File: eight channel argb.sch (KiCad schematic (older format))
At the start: 13 parts, among them J1 Conn_01x03, J10 Conn_01x06_Male, J2 Conn_01x03, J3 Conn_01x03, J4 Conn_01x03, J5 Conn_01x03, J6 Conn_01x03, J7 Conn_01x03, J8 Conn_01x03, J9 Conn_01x06_Male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

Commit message: Remove 6-pin SATA power connectors and replace with 4-pin "Molex" socket.
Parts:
- removed J10, J9: Conn_01x06_Male, Connector_JST:JST_XH_S6B-XH-A_1x06_P2.50mm_Horizontal, symbol Connector:Conn_01x06_Male
- added J?: 350211-1, 3502111, symbol SamacSys:350211-1
- J1, J2, J3, J4, J5, J6, J7, J8: symbol Connector_Generic:Conn_01x03 -> eight-channel-argb-rescue:Conn_01x03-Connector_Generic
- SW1: symbol Switch:SW_DIP_x01 -> eight-channel-argb-rescue:SW_DIP_x01-Switch
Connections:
- wire segments 138 -> 113
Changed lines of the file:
@@
 $EndComp
 $Comp
-L Connector_Generic:Conn_01x03 J2
+L eight-channel-argb-rescue:Conn_01x03-Connector_Generic J2
 U 1 1 5FF2A38F
 P 7350 2600
@@
 F 3 "https://aliexpress.com/item/32864722159.html" H 2800 5150 50  0001 C CNN
 	1    3250 3800
-	1    0    0    -1
-$EndComp
-$Comp
-L power:+5V #PWR01
-U 1 1 5FF37571
-P 4700 1500
-F 0 "#PWR01" H 4700 1350 50  0001 C CNN
-F 1 "+5V" H 4715 1673 50  0000 C CNN
-F 2 "" H 4700 1500 50  0001 C CNN
-F 3 "" H 4700 1500 50  0001 C CNN
-	1    4700 1500
-	1    0    0    -1
-$EndComp
-$Comp
-L power:GND #PWR02
-U 1 1 5FF37BFD
-P 5200 1200
-F 0 "#PWR02" H 5200 950 50  0001 C CNN
-F 1 "GND" H 5205 1027 50  0000 C CNN
-F 2 "" H 5200 1200 50  0001 C CNN
-F 3 "" H 5200 1200 50  0001 C CNN
-	1    5200 1200
 	1    0    0    -1
 $EndComp
@@
 NoConn ~ 3250 5200
 $Comp
-L Connector_Generic:Conn_01x03 J1
+L eight-channel-argb-rescue:Conn_01x03-Connector_Generic J1
 U 1 1 5FF476B4
 P 7350 2200
@@
 $EndComp
 $Comp
-L Connector_Generic:Conn_01x03 J7
+L eight-channel-argb-rescue:Conn_01x03-Connector_Generic J7
 U 1 1 5FF47C5F
 P 7350 4600
@@
 $EndComp
 $Comp
-L Connector_Generic:Conn_01x03 J6
+L eight-channel-argb-rescue:Conn_01x03-Connector_Generic J6
 U 1 1 5FF4879A
 P 7350 4200
@@
 $EndComp
 $Comp
-L Connector_Generic:Conn_01x03 J5
+L eight-channel-argb-rescue:Conn_01x03-Connector_Generic J5
 U 1 1 5FF48D18
 P 7350 3800
@@
 $EndComp
 $Comp
-L Connector_Generic:Conn_01x03 J4
+L eight-channel-argb-rescue:Conn_01x03-Connector_Generic J4
 U 1 1 5FF49041
 P 7350 3400
@@
 $EndComp
 $Comp
-L Connector_Generic:Conn_01x03 J3
+L eight-channel-argb-rescue:Conn_01x03-Connector_Generic J3
 U 1 1 5FF495A2
 P 7350 3000
@@
 $EndComp
 $Comp
-L Connector_Generic:Conn_01x03 J8
+L eight-channel-argb-rescue:Conn_01x03-Connector_Generic J8
 U 1 1 5FF4A43D
 P 7350 5000
@@
 	6900 5100 7150 5100
 Wire Wire Line
-	4950 2100 5200 2100
-Wire Wire Line
 	7150 4700 6900 4700
 Connection ~ 6900 4700
@@
 Wire Wire Line
 	6350 5000 6350 3750
-$Comp
-L power:PWR_FLAG #FLG02
-U 1 1 5FF6F199
-P 4700 1850
-F 0 "#FLG02" H 4700 1925 50  0001 C CNN
-F 1 "PWR_FLAG" H 4450 1850 50  0000 C CNN
-F 2 "" H 4700 1850 50  0001 C CNN
-F 3 "~" H 4700 1850 50  0001 C CNN
-	1    4700 1850
-	1    0    0    -1
-$EndComp
 Wire Wire Line
 	4550 2150 4700 2150
-Wire Wire Line
-	4700 1500 4700 1850
-Connection ~ 4700 1850
-Wire Wire Line
-	4700 1850 4700 1950
-Wire Wire Line
-	7000 1850 6700 1850
 Wire Wire Line
 	4900 1850 4900 1950
@@
 	4900 1950 4700 1950
 Connection ~ 4700 1950
-Wire Wire Line
-	4700 1950 4700 2150
-Wire Wire Line
-	5200 1550 5200 1650
-Connection ~ 5200 2100
-Wire Wire Line
-	5200 1550 5450 1550
-Wire Wire Line
-	5450 1550 5450 1500
-Wire Wire Line
-	5450 1200 5200 1200
-$Comp
-L power:PWR_FLAG #FLG03
-U 1 1 5FF8D592
-P 5450 1500
-F 0 "#FLG03" H 5450 1575 50  0001 C CNN
-F 1 "PWR_FLAG" H 5200 1500 50  0000 C CNN
-F 2 "" H 5450 1500 50  0001 C CNN
-F 3 "~" H 5450 1500 50  0001 C CNN
-	1    5450 1500
-	1    0    0    -1
-$EndComp
-Connection ~ 5450 1500
-Wire Wire Line
-	5450 1500 5450 1200
-Connection ~ 6700 1850
-Wire Wire Line
-	6800 1700 6800 2100
-Connection ~ 6800 2100
-Wire Wire Line
-	6800 2100 6900 2100
-$Comp
-L Switch:SW_DIP_x01 SW1
+$Comp
+L eight-channel-argb-rescue:SW_DIP_x01-Switch SW1
 U 1 1 5FFD2886
 P 3800 1950
@@
 	4100 1950 4700 1950
 $Comp
-L power:PWR_FLAG #FLG01
+L eight-channel-argb-rescue:PWR_FLAG-power #FLG01
 U 1 1 5FF41B16
 P 3250 1950
@@
 	3250 1950 3500 1950
 $Comp
-L Connector:Conn_01x06_Male J9
-U 1 1 5FF69EE1
-P 6050 1200
-F 0 "J9" V 6112 1444 50  0000 L CNN
-F 1 "Conn_01x06_Male" V 6203 1444 50  0000 L CNN
-F 2 "Connector_JST:JST_XH_S6B-XH-A_1x06_P2.50mm_Horizontal" H 6050 1200 50  0001 C CNN
-F 3 "~" H 6050 1200 50  0001 C CNN
-	1    6050 1200
-	0    1    1    0
-$EndComp
-$Comp
-L Connector:Conn_01x06_Male J10
-U 1 1 5FF6B11B
-P 7400 1200
-F 0 "J10" V 7462 1444 50  0000 L CNN
-F 1 "Conn_01x06_Male" V 7553 1444 50  0000 L CNN
-F 2 "Connector_JST:JST_XH_S6B-XH-A_1x06_P2.50mm_Horizontal" H 7400 1200 50  0001 C CNN
-F 3 "~" H 7400 1200 50  0001 C CNN
-	1    7400 1200
-	0    1    1    0
-$EndComp
-Wire Wire Line
-	6700 1600 6700 1850
-Wire Wire Line
-	5200 2100 6800 2100
-Wire Wire Line
-	4900 1850 6700 1850
-Wire Wire Line
-	6700 1600 6250 1600
-Wire Wire Line
-	6050 1600 6050 1400
-Wire Wire Line
-	6150 1600 6150 1400
-Connection ~ 6150 1600
-Wire Wire Line
-	6150 1600 6050 1600
-Wire Wire Line
-	6250 1600 6250 1400
-Connection ~ 6250 1600
-Wire Wire Line
-	6250 1600 6150 1600
-Wire Wire Line
-	5200 1650 5750 1650
-Wire Wire Line
-	5750 1650 5750 1400
-Connection ~ 5200 1650
-Wire Wire Line
-	5200 1650 5200 2100
-Wire Wire Line
-	5750 1650 5850 1650
-Wire Wire Line
-	5850 1650 5850 1400
-Connection ~ 5750 1650
-Wire Wire Line
-	5850 1650 5950 1650
-Wire Wire Line
-	5950 1650 5950 1400
-Connection ~ 5850 1650
-Wire Wire Line
-	6800 1700 7100 1700
-Wire Wire Line
-	7100 1700 7100 1450
-Wire Wire Line
-	7100 1450 7200 1450
-Wire Wire Line
-	7200 1450 7200 1400
-Connection ~ 7100 1450
-Wire Wire Line
-	7100 1450 7100 1400
-Wire Wire Line
-	7200 1450 7300 1450
-Wire Wire Line
-	7300 1450 7300 1400
-Connection ~ 7200 1450
-Wire Wire Line
-	7000 1850 7400 1850
-Wire Wire Line
-	7400 1850 7400 1400
-Connection ~ 7000 1850
-Wire Wire Line
-	7400 1400 7500 1400
-Connection ~ 7400 1400
-Wire Wire Line
-	7400 1400 7500 1400
-Connection ~ 7500 1400
-Wire Wire Line
-	7500 1400 7600 1400
+L SamacSys:350211-1 J?
+U 1 1 6053820E
+P 5300 1300
+F 0 "J?" H 5928 1196 50  0000 L CNN
+F 1 "350211-1" H 5928 1105 50  0000 L CNN
+F 2 "3502111" H 5950 1400 50  0001 L CNN
+F 3 "http://uk.rs-online.com/web/p/products/0471430" H 5950 1300 50  0001 L CNN
+F 4 "Pin & Socket Connectors CONN PCM 4 POS TIN" H 5950 1200 50  0001 L CNN "Description"
+F 5 "10.29" H 5950 1100 50  0001 L CNN "Height"
+F 6 "0471430" H 5950 1000 50  0001 L CNN "RS Part Number"
+F 7 "http://uk.rs-online.com/web/p/products/0471430" H 5950 900 50  0001 L CNN "RS Price/Stock"
+F 8 "TE Connectivity" H 5950 800 50  0001 L CNN "Manufacturer_Name"
+F 9 "350211-1" H 5950 700 50  0001 L CNN "Manufacturer_Part_Number"
+	1    5300 1300
+	1    0    0    -1
+$EndComp
+Wire Wire Line
+	4900 1850 5000 1850
+Connection ~ 5200 2100
+Wire Wire Line
+	5200 2100 6900 2100
+Wire Wire Line
+	4950 2100 5200 2100
+Wire Wire Line
+	4700 1950 4700 2150
+Connection ~ 5000 1850
+Wire Wire Line
+	5000 1850 7000 1850
+Wire Wire Line
+	5300 1600 5000 1600
+Wire Wire Line
+	5300 1500 5200 1500
+Connection ~ 5200 1500
+Wire Wire Line
+	5300 1400 5200 1400
+Wire Wire Line
+	5200 1400 5200 1500
+Wire Wire Line
+	5200 1500 5200 2100
+Wire Wire Line
+	5000 1600 5000 1850
+$Comp
+L eight-channel-argb-rescue:PWR_FLAG-power #FLG03
+U 1 1 5FF8D592
+P 5200 1050
+F 0 "#FLG03" H 5200 1125 50  0001 C CNN
+F 1 "PWR_FLAG" H 4950 1050 50  0000 C CNN
+F 2 "" H 5200 1050 50  0001 C CNN
+F 3 "~" H 5200 1050 50  0001 C CNN
+	1    5200 1050
+	1    0    0    -1
+$EndComp
+Connection ~ 5200 1050
+Connection ~ 5000 950
+Wire Wire Line
+	5200 1050 5200 1400
+Wire Wire Line
+	5000 950  5000 1600
+$Comp
+L eight-channel-argb-rescue:GND-power #PWR02
+U 1 1 5FF37BFD
+P 5200 850
+F 0 "#PWR02" H 5200 600 50  0001 C CNN
+F 1 "GND" H 5205 677 50  0000 C CNN
+F 2 "" H 5200 850 50  0001 C CNN
+F 3 "" H 5200 850 50  0001 C CNN
+	1    5200 850
+	-1   0    0    1
+$EndComp
+$Comp
+L eight-channel-argb-rescue:PWR_FLAG-power #FLG02
+U 1 1 5FF6F199
+P 5000 950
+F 0 "#FLG02" H 5000 1025 50  0001 C CNN
+F 1 "PWR_FLAG" H 4750 950 50  0000 C CNN
+F 2 "" H 5000 950 50  0001 C CNN
+F 3 "~" H 5000 950 50  0001 C CNN
+	1    5000 950
+	1    0    0    -1
+$EndComp
+Wire Wire Line
+	5200 1050 5200 850
+Wire Wire Line
+	5000 850  5000 950
+$Comp
+L eight-channel-argb-rescue:+5V-power #PWR01
+U 1 1 5FF37571
+P 5000 850
+F 0 "#PWR01" H 5000 700 50  0001 C CNN
+F 1 "+5V" H 5015 1023 50  0000 C CNN
+F 2 "" H 5000 850 50  0001 C CNN
+F 3 "" H 5000 850 50  0001 C CNN
+	1    5000 850
+	1    0    0    -1
+$EndComp
+Connection ~ 5200 1400
+Connection ~ 5000 1600
 $EndSCHEMATC

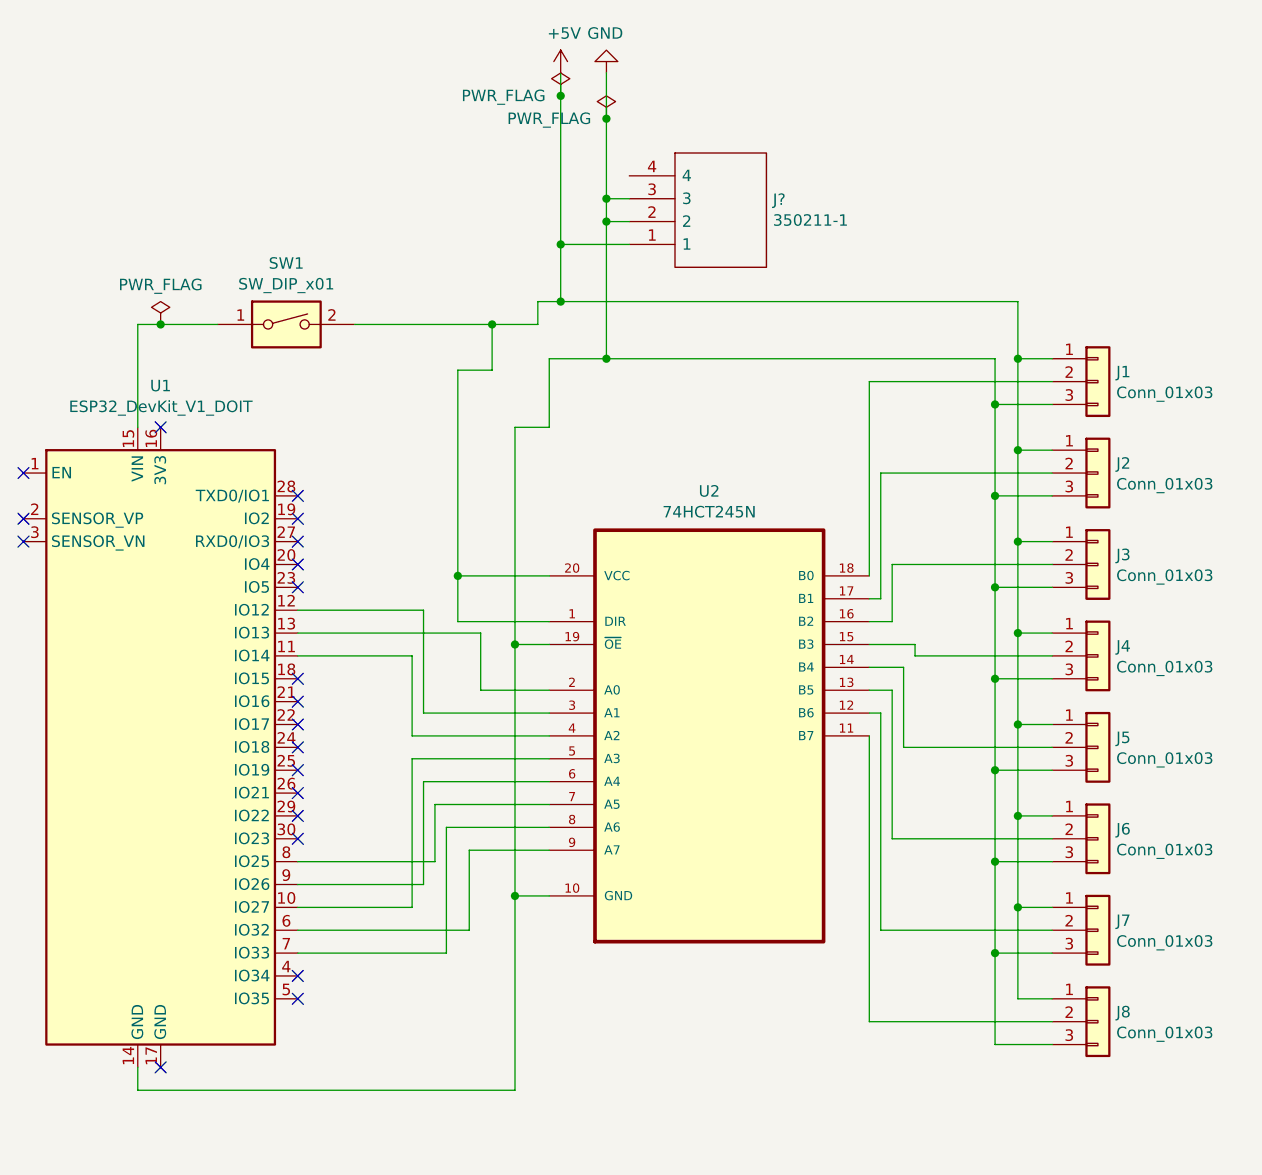
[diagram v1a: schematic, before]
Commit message: Clean up the wire lines.
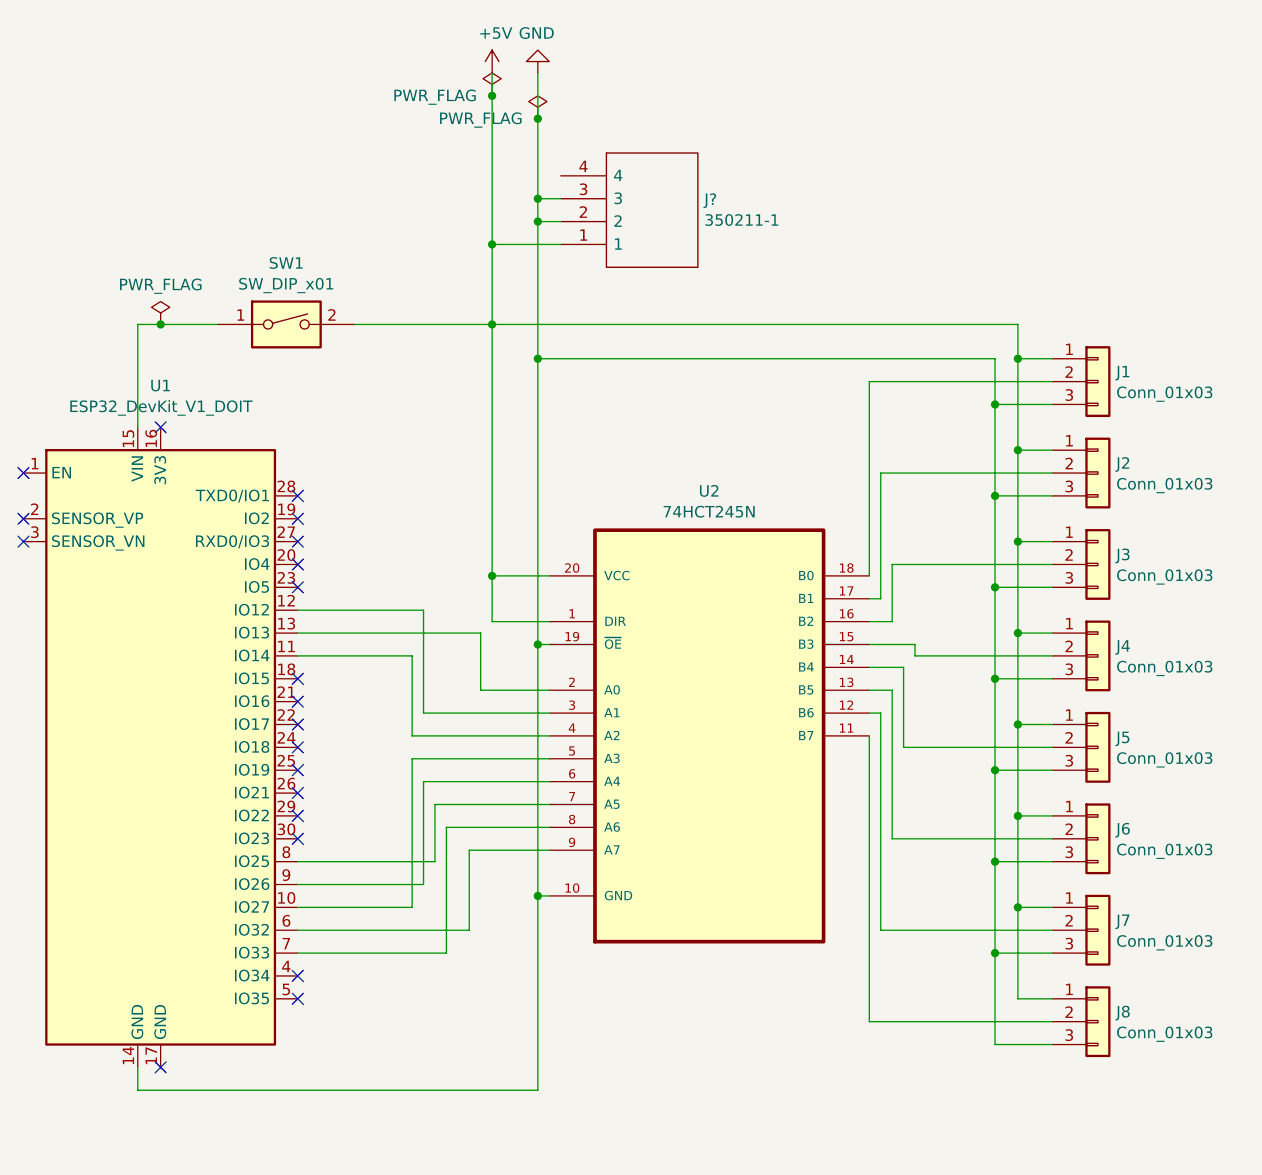
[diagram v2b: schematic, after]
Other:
- moved on the sheet: J?
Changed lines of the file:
@@
 $EndComp
 Wire Wire Line
-	4550 2150 4550 3050
-Wire Wire Line
-	4550 3050 4950 3050
-Wire Wire Line
-	4950 3250 4550 3250
-Wire Wire Line
-	4550 3250 4550 3050
-Connection ~ 4550 3050
-Wire Wire Line
-	4950 2100 4950 2400
-Wire Wire Line
-	4950 2400 4800 2400
-Wire Wire Line
-	4800 2400 4800 3350
-Wire Wire Line
-	4800 3350 4950 3350
-Wire Wire Line
-	4950 4450 4800 4450
-Wire Wire Line
-	4800 4450 4800 3350
-Connection ~ 4800 3350
+	4950 3250 4700 3250
+Wire Wire Line
+	4950 4450 4900 4450
 Wire Wire Line
 	3850 3300 4650 3300
@@
 NoConn ~ 2650 2900
 NoConn ~ 3250 2400
-Connection ~ 4800 4450
 Wire Wire Line
 	3150 5200 3150 5300
-Wire Wire Line
-	3150 5300 4800 5300
-Wire Wire Line
-	4800 4450 4800 5300
 NoConn ~ 3250 5200
 $Comp
@@
 $EndComp
 Wire Wire Line
-	7000 1850 7000 2100
+	7000 1950 7000 2100
 Wire Wire Line
 	7000 4900 7150 4900
@@
 Wire Wire Line
 	6350 5000 6350 3750
-Wire Wire Line
-	4550 2150 4700 2150
-Wire Wire Line
-	4900 1850 4900 1950
-Wire Wire Line
-	4900 1950 4700 1950
-Connection ~ 4700 1950
 $Comp
 L eight-channel-argb-rescue:SW_DIP_x01-Switch SW1
@@
 Wire Wire Line
 	3150 1950 3150 2400
-Wire Wire Line
-	4100 1950 4700 1950
 $Comp
 L eight-channel-argb-rescue:PWR_FLAG-power #FLG01
@@
 L SamacSys:350211-1 J?
 U 1 1 6053820E
-P 5300 1300
-F 0 "J?" H 5928 1196 50  0000 L CNN
-F 1 "350211-1" H 5928 1105 50  0000 L CNN
-F 2 "3502111" H 5950 1400 50  0001 L CNN
-F 3 "http://uk.rs-online.com/web/p/products/0471430" H 5950 1300 50  0001 L CNN
-F 4 "Pin & Socket Connectors CONN PCM 4 POS TIN" H 5950 1200 50  0001 L CNN "Description"
-F 5 "10.29" H 5950 1100 50  0001 L CNN "Height"
-F 6 "0471430" H 5950 1000 50  0001 L CNN "RS Part Number"
-F 7 "http://uk.rs-online.com/web/p/products/0471430" H 5950 900 50  0001 L CNN "RS Price/Stock"
-F 8 "TE Connectivity" H 5950 800 50  0001 L CNN "Manufacturer_Name"
-F 9 "350211-1" H 5950 700 50  0001 L CNN "Manufacturer_Part_Number"
-	1    5300 1300
-	1    0    0    -1
-$EndComp
-Wire Wire Line
-	4900 1850 5000 1850
-Connection ~ 5200 2100
-Wire Wire Line
-	5200 2100 6900 2100
-Wire Wire Line
-	4950 2100 5200 2100
-Wire Wire Line
-	4700 1950 4700 2150
-Connection ~ 5000 1850
-Wire Wire Line
-	5000 1850 7000 1850
-Wire Wire Line
-	5300 1600 5000 1600
-Wire Wire Line
-	5300 1500 5200 1500
-Connection ~ 5200 1500
-Wire Wire Line
-	5300 1400 5200 1400
-Wire Wire Line
-	5200 1400 5200 1500
-Wire Wire Line
-	5200 1500 5200 2100
-Wire Wire Line
-	5000 1600 5000 1850
+P 5000 1300
+F 0 "J?" H 5628 1196 50  0000 L CNN
+F 1 "350211-1" H 5628 1105 50  0000 L CNN
+F 2 "3502111" H 5650 1400 50  0001 L CNN
+F 3 "http://uk.rs-online.com/web/p/products/0471430" H 5650 1300 50  0001 L CNN
+F 4 "Pin & Socket Connectors CONN PCM 4 POS TIN" H 5650 1200 50  0001 L CNN "Description"
+F 5 "10.29" H 5650 1100 50  0001 L CNN "Height"
+F 6 "0471430" H 5650 1000 50  0001 L CNN "RS Part Number"
+F 7 "http://uk.rs-online.com/web/p/products/0471430" H 5650 900 50  0001 L CNN "RS Price/Stock"
+F 8 "TE Connectivity" H 5650 800 50  0001 L CNN "Manufacturer_Name"
+F 9 "350211-1" H 5650 700 50  0001 L CNN "Manufacturer_Part_Number"
+	1    5000 1300
+	1    0    0    -1
+$EndComp
+Wire Wire Line
+	5000 1600 4700 1600
+Wire Wire Line
+	5000 1500 4900 1500
+Connection ~ 4900 1500
+Wire Wire Line
+	5000 1400 4900 1400
+Wire Wire Line
+	4900 1400 4900 1500
+Wire Wire Line
+	4900 1500 4900 2100
+Wire Wire Line
+	4700 1600 4700 1950
 $Comp
 L eight-channel-argb-rescue:PWR_FLAG-power #FLG03
 U 1 1 5FF8D592
-P 5200 1050
-F 0 "#FLG03" H 5200 1125 50  0001 C CNN
-F 1 "PWR_FLAG" H 4950 1050 50  0000 C CNN
-F 2 "" H 5200 1050 50  0001 C CNN
-F 3 "~" H 5200 1050 50  0001 C CNN
-	1    5200 1050
-	1    0    0    -1
-$EndComp
-Connection ~ 5200 1050
-Connection ~ 5000 950
-Wire Wire Line
-	5200 1050 5200 1400
-Wire Wire Line
-	5000 950  5000 1600
+P 4900 1050
+F 0 "#FLG03" H 4900 1125 50  0001 C CNN
+F 1 "PWR_FLAG" H 4650 1050 50  0000 C CNN
+F 2 "" H 4900 1050 50  0001 C CNN
+F 3 "~" H 4900 1050 50  0001 C CNN
+	1    4900 1050
+	1    0    0    -1
+$EndComp
+Connection ~ 4900 1050
+Connection ~ 4700 950
+Wire Wire Line
+	4900 1050 4900 1400
+Wire Wire Line
+	4700 950  4700 1600
 $Comp
 L eight-channel-argb-rescue:GND-power #PWR02
 U 1 1 5FF37BFD
-P 5200 850
-F 0 "#PWR02" H 5200 600 50  0001 C CNN
-F 1 "GND" H 5205 677 50  0000 C CNN
-F 2 "" H 5200 850 50  0001 C CNN
-F 3 "" H 5200 850 50  0001 C CNN
-	1    5200 850
+P 4900 850
+F 0 "#PWR02" H 4900 600 50  0001 C CNN
+F 1 "GND" H 4905 677 50  0000 C CNN
+F 2 "" H 4900 850 50  0001 C CNN
+F 3 "" H 4900 850 50  0001 C CNN
+	1    4900 850
 	-1   0    0    1
 $EndComp
@@
 L eight-channel-argb-rescue:PWR_FLAG-power #FLG02
 U 1 1 5FF6F199
-P 5000 950
-F 0 "#FLG02" H 5000 1025 50  0001 C CNN
-F 1 "PWR_FLAG" H 4750 950 50  0000 C CNN
-F 2 "" H 5000 950 50  0001 C CNN
-F 3 "~" H 5000 950 50  0001 C CNN
-	1    5000 950
-	1    0    0    -1
-$EndComp
-Wire Wire Line
-	5200 1050 5200 850
-Wire Wire Line
-	5000 850  5000 950
+P 4700 950
+F 0 "#FLG02" H 4700 1025 50  0001 C CNN
+F 1 "PWR_FLAG" H 4450 950 50  0000 C CNN
+F 2 "" H 4700 950 50  0001 C CNN
+F 3 "~" H 4700 950 50  0001 C CNN
+	1    4700 950
+	1    0    0    -1
+$EndComp
+Wire Wire Line
+	4900 1050 4900 850
+Wire Wire Line
+	4700 850  4700 950
 $Comp
 L eight-channel-argb-rescue:+5V-power #PWR01
 U 1 1 5FF37571
-P 5000 850
-F 0 "#PWR01" H 5000 700 50  0001 C CNN
-F 1 "+5V" H 5015 1023 50  0000 C CNN
-F 2 "" H 5000 850 50  0001 C CNN
-F 3 "" H 5000 850 50  0001 C CNN
-	1    5000 850
-	1    0    0    -1
-$EndComp
-Connection ~ 5200 1400
-Connection ~ 5000 1600
+P 4700 850
+F 0 "#PWR01" H 4700 700 50  0001 C CNN
+F 1 "+5V" H 4715 1023 50  0000 C CNN
+F 2 "" H 4700 850 50  0001 C CNN
+F 3 "" H 4700 850 50  0001 C CNN
+	1    4700 850
+	1    0    0    -1
+$EndComp
+Connection ~ 4900 1400
+Connection ~ 4700 1600
+Connection ~ 4700 1950
+Connection ~ 4900 2100
+Wire Wire Line
+	4900 2100 6900 2100
+Wire Wire Line
+	4700 1950 7000 1950
+Wire Wire Line
+	4900 2100 4900 3350
+Connection ~ 4900 4450
+Wire Wire Line
+	4900 4450 4900 5300
+Wire Wire Line
+	3150 5300 4900 5300
+Wire Wire Line
+	4700 1950 4700 3050
+Connection ~ 4700 3050
+Wire Wire Line
+	4700 3050 4950 3050
+Wire Wire Line
+	4100 1950 4700 1950
+Wire Wire Line
+	4700 3050 4700 3250
+Connection ~ 4900 3350
+Wire Wire Line
+	4900 3350 4950 3350
+Wire Wire Line
+	4900 3350 4900 4450
 $EndSCHEMATC
